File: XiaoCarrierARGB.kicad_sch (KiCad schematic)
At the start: 1 part, among them U1 XIAO-ESP32-C6-DIP

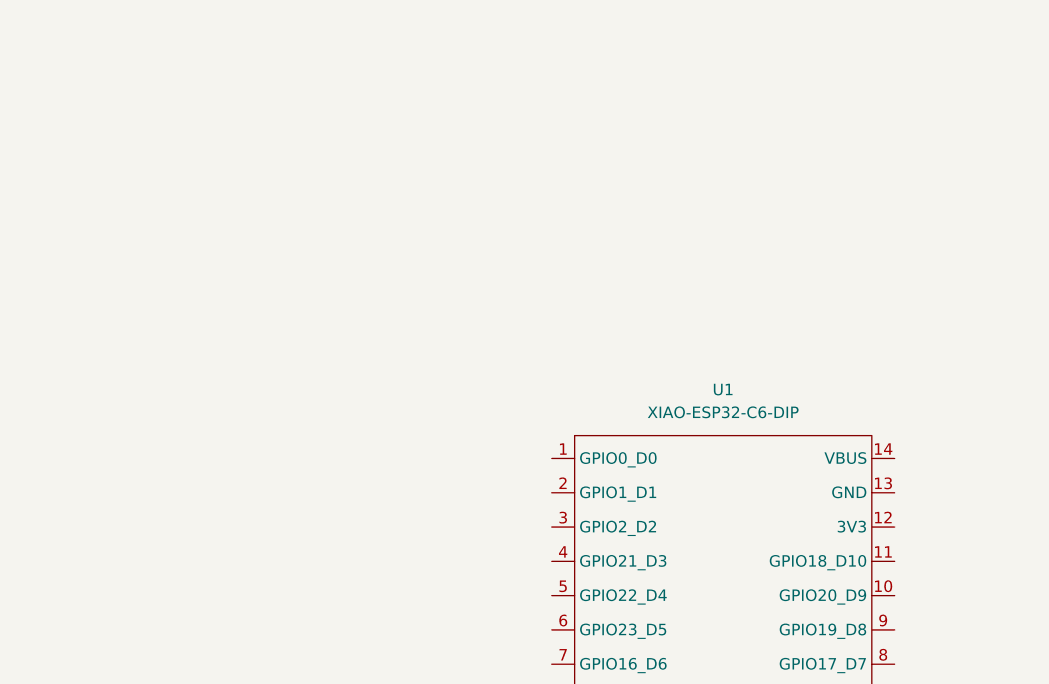
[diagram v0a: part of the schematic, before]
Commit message: Added Buck
TPP362081 added to library and schematic, might switch exact model from TPP362081 to TPP362083
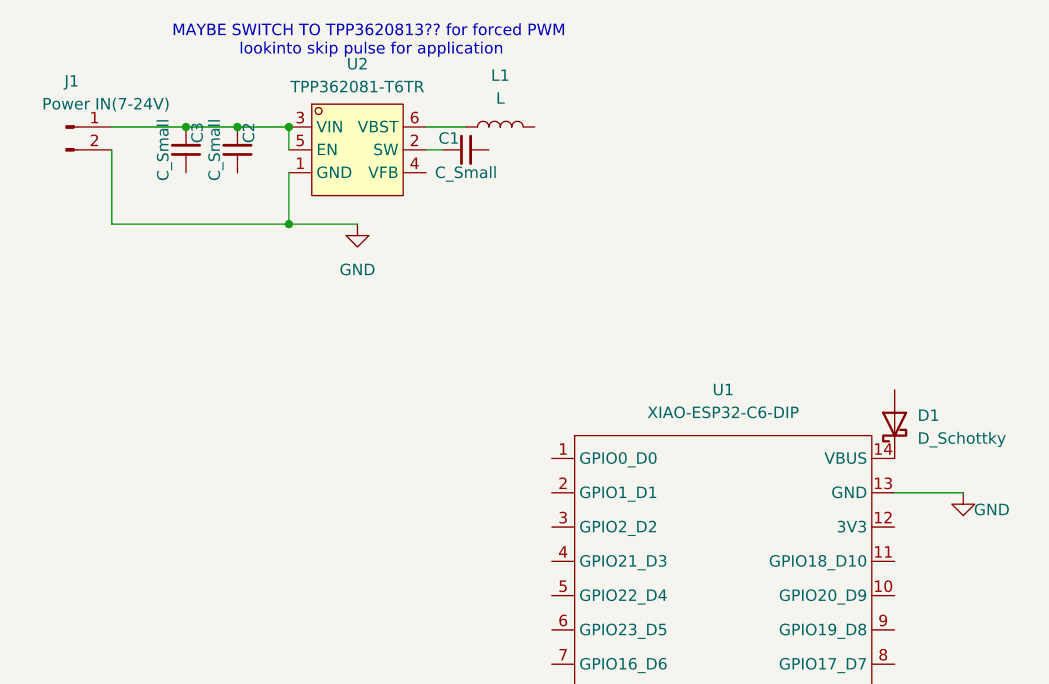
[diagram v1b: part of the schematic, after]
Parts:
- added C1, C2, C3: C_Small, Package_QFP:TQFP-44_10x10mm_P0.8mm, symbol Device:C_Small
- added D1: D_Schottky, Package_SON:WSON-8-1EP_6x5mm_P1.27mm_EP3.4x4mm, symbol Device:D_Schottky
- added J1: Power IN(7-24V), LED_THT:LED_D5.0mm_IRGrey, symbol Connector:Conn_01x02_Pin
- added L1: L, symbol Device:L
- added U2: TPP362081-T6TR, Package_TO_SOT_SMD:TSOT-23-6, symbol EasyEDA:TPP362081-T6TR
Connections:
- net GND: now reaches U1.13 (GND)
- net GND: now also J1.2 (Pin_2), U2.1 (GND)
- net at U1.14 (VBUS): now also D1.1 (K)
- new net: L1.1, U2.6 (VBST)
- new net: C1.1, U2.2 (SW)
- new net: C2.1, C3.1, J1.1 (Pin_1), U2.3 (VIN), U2.5 (EN)
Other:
- note added: "MAYBE SWITCH TO TPP3620813?? for forced PWM lookinto skip pulse for application"

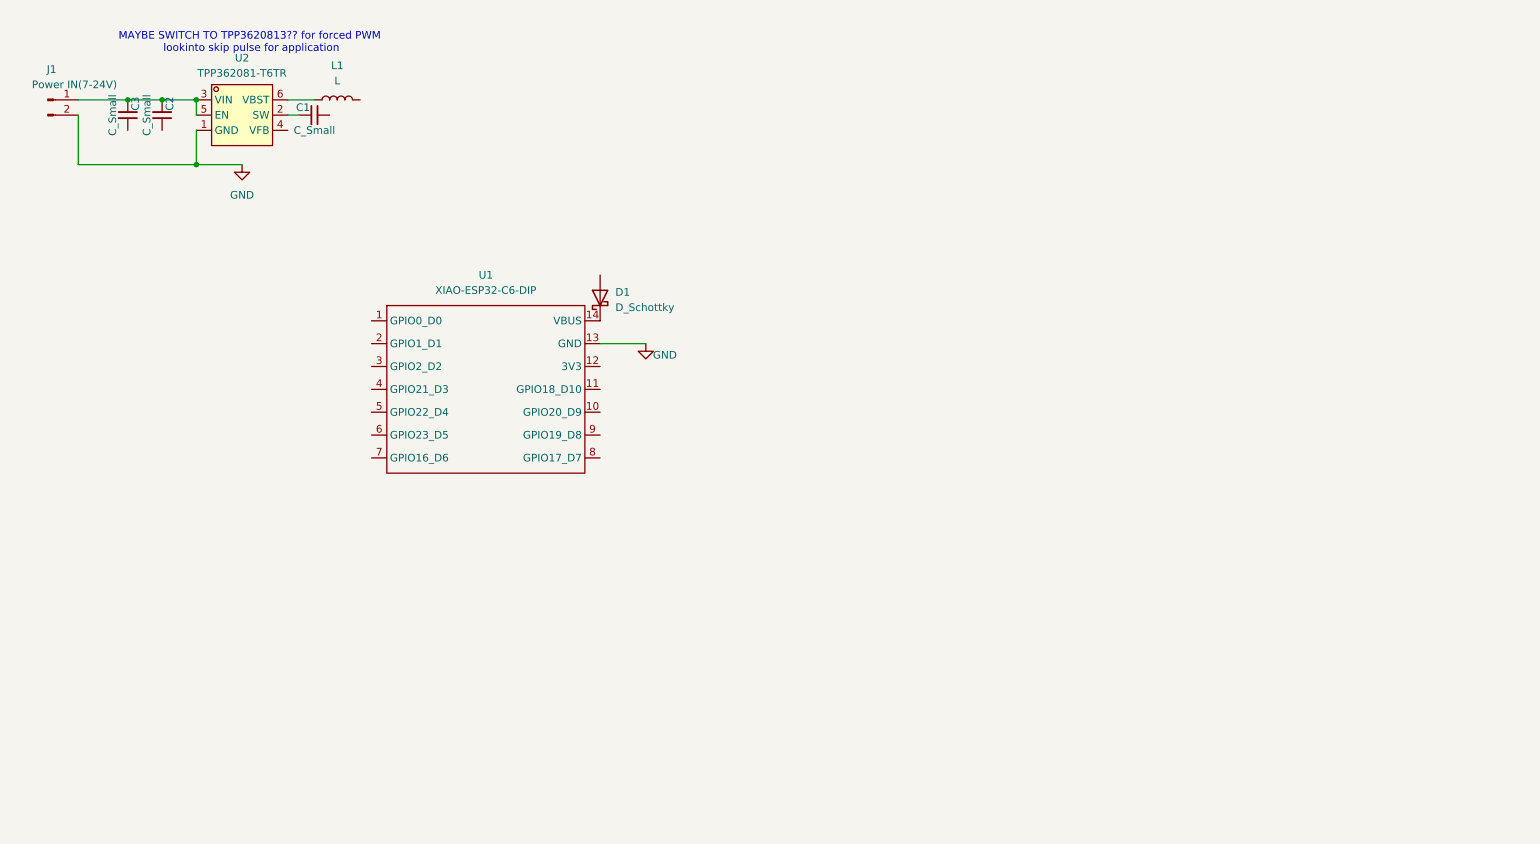
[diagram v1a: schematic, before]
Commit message: added LDO and level shifters.
most footprint assingments done, need to source ptc fuse and decide on if pullups or pulldowns should be placed but not populated for versatility
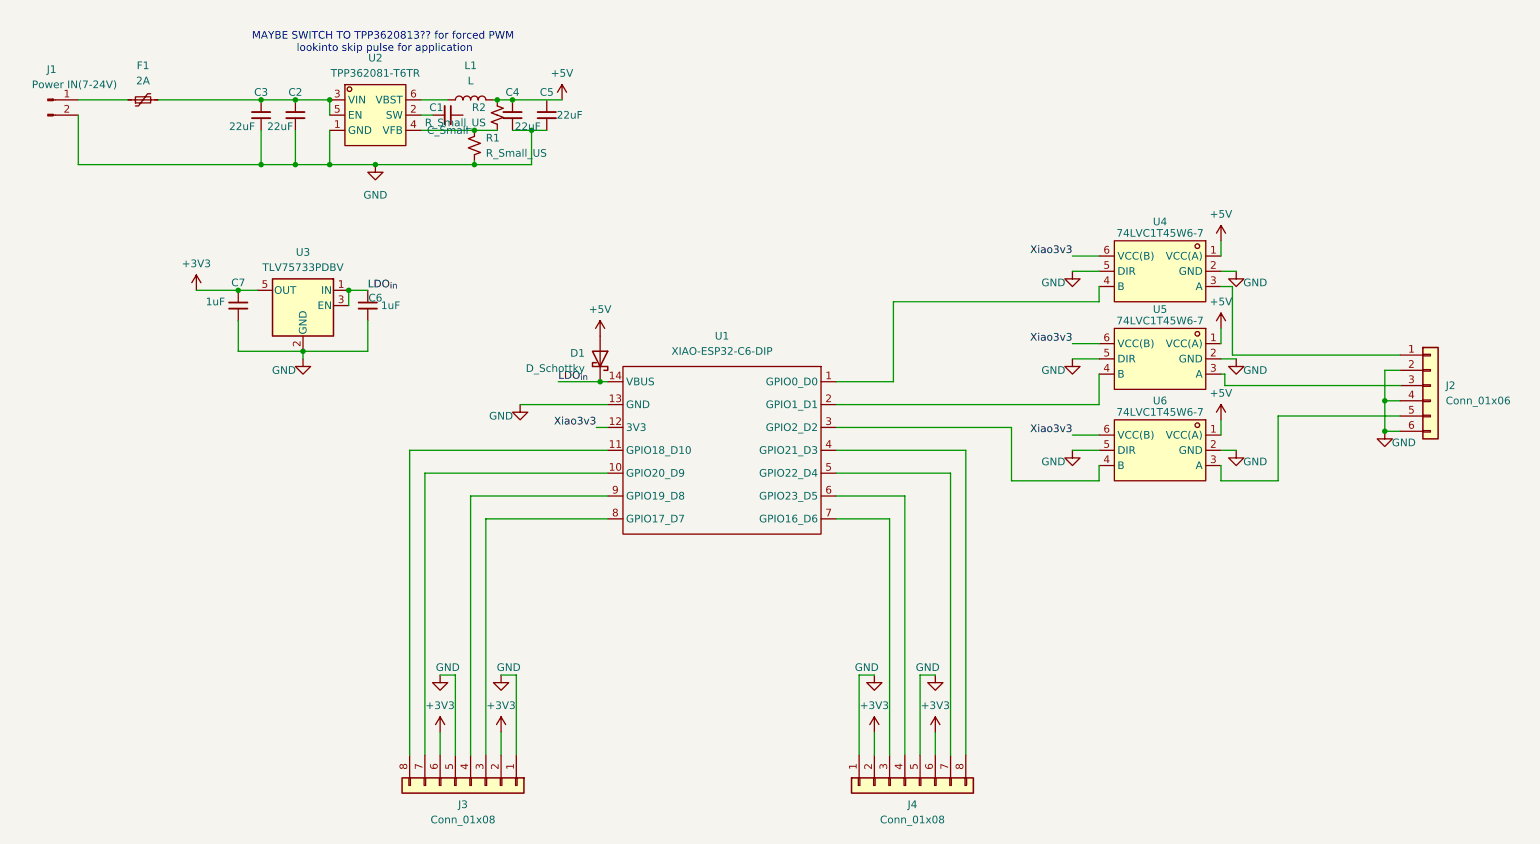
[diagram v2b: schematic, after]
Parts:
- added C4, C5: 22uF, Capacitor_SMD:C_0805_2012Metric_Pad1.18x1.45mm_HandSolder, symbol Device:C_Small
- added C6, C7: 1uF, Capacitor_SMD:C_0805_2012Metric_Pad1.18x1.45mm_HandSolder, symbol Device:C_Small
- added F1: 2A, symbol Device:Polyfuse_Small
- added J2: Conn_01x06, Connector_RJ:RJ45_Abracon_ARJP11A-MA_Horizontal, symbol Connector_Generic:Conn_01x06
- added J3, J4: Conn_01x08, Connector_RJ:RJ45_Abracon_ARJP11A-MA_Horizontal, symbol Connector_Generic:Conn_01x08
- added R1, R2: R_Small_US, Resistor_THT:R_Array_SIP4, symbol Device:R_Small_US
- added U3: TLV75733PDBV, Package_TO_SOT_SMD:SOT-23-5, symbol Regulator_Linear:TLV75733PDBV
- added U4, U5, U6: 74LVC1T45W6-7, Package_TO_SOT_SMD:SOT-23-6, symbol EasyEDA:74LVC1T45W6-7
- C1: footprint Package_QFP:TQFP-44_10x10mm_P0.8mm -> Capacitor_SMD:C_0805_2012Metric_Pad1.18x1.45mm_HandSolder
- C2, C3: value C_Small -> 22uF; footprint Package_QFP:TQFP-44_10x10mm_P0.8mm -> Capacitor_SMD:C_0805_2012Metric_Pad1.18x1.45mm_HandSolder
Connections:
- net GND: now also C2.2, C3.2, C4.2, C5.2, C6.2, C7.2, J2.2 (Pin_2), J2.4 (Pin_4), J2.6 (Pin_6), J3.1 (Pin_1), J3.5 (Pin_5), J4.1 (Pin_1), J4.5 (Pin_5), R1.2, U3.2 (GND), U4.2 (GND), U4.5 (DIR), U5.2 (GND), U5.5 (DIR), U6.2 (GND), U6.5 (DIR)
- net at U1.1 (GPIO0_D0): now also U4.4 (B)
- net at U1.10 (GPIO20_D9): now also J3.7 (Pin_7)
- net at U1.11 (GPIO18_D10): now also J3.8 (Pin_8)
- net Xiao3v3: now reaches U1.12 (3V3)
- net Xiao3v3: now also U4.6 (VCC(B)), U5.6 (VCC(B)), U6.6 (VCC(B))
- net LDO_{in}: now reaches D1.1 (K), U1.14 (VBUS)
- net LDO_{in}: now also C6.1, U3.1 (IN), U3.3 (EN)
- net at U1.2 (GPIO1_D1): now also U5.4 (B)
- net at U1.3 (GPIO2_D2): now also U6.4 (B)
- net at U1.4 (GPIO21_D3): now also J4.8 (Pin_8)
- net at U1.5 (GPIO22_D4): now also J4.7 (Pin_7)
- net at U1.6 (GPIO23_D5): now also J4.4 (Pin_4)
- net at U1.7 (GPIO16_D6): now also J4.3 (Pin_3)
- net at U1.8 (GPIO17_D7): now also J3.3 (Pin_3)
- net at U1.9 (GPIO19_D8): now also J3.4 (Pin_4)
- net +5V: now reaches L1.2
- net +5V: now also D1.2 (A), C4.1, R2.1, U4.1 (VCC(A)), U5.1 (VCC(A)), U6.1 (VCC(A))
- net at C2.1, C3.1, U2.3 (VIN)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: now also F1.2; no longer J1.1 (Pin_1)
- net at U2.4 (VFB): now also R1.1, R2.2
- new net: J2.1 (Pin_1), U4.3 (A)
- new net: J2.3 (Pin_3), U5.3 (A)
- new net: F1.1, J1.1 (Pin_1)
- new net: J2.5 (Pin_5), U6.3 (A)
- new net +3V3: C7.1, J3.2 (Pin_2), J3.6 (Pin_6), J4.2 (Pin_2), J4.6 (Pin_6), U3.5 (OUT)
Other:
- moved on the sheet: C1, C2, C3, D1, L1, U1, U2

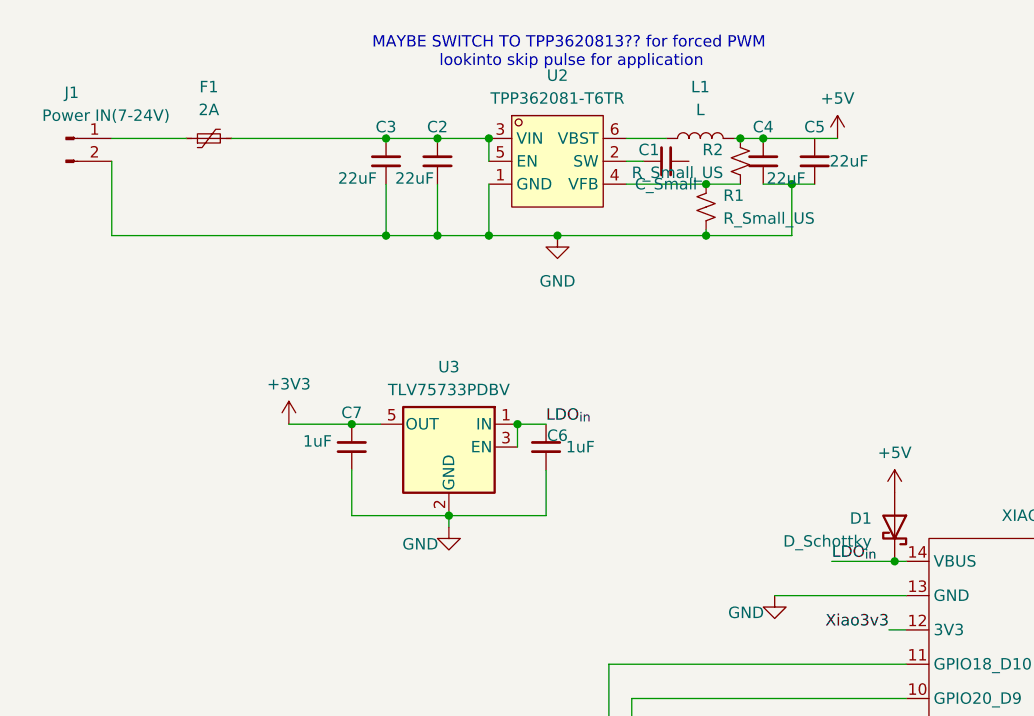
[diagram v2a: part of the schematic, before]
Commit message: Sourced PTC fuse
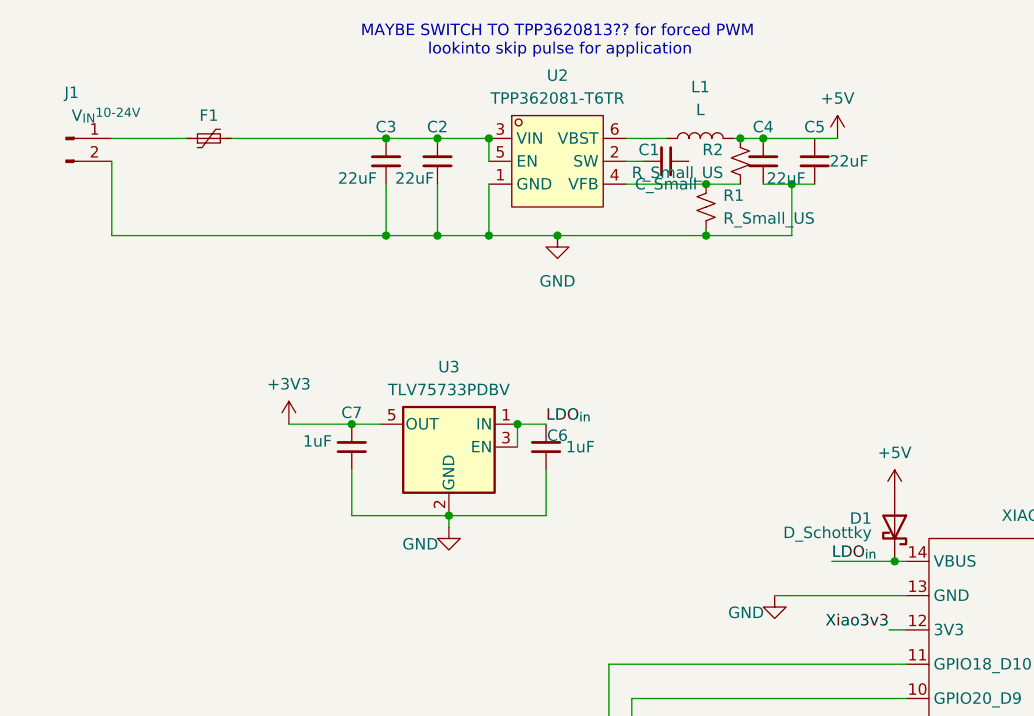
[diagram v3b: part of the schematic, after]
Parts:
- F1: value 2A -> YAGEO SMD1812B110TF/33; footprint (none) -> Fuse:Fuse_1812_4532Metric
- J1: value Power IN(7-24V) -> V_{IN}^{10-24V}
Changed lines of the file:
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@@
 	(text "MAYBE SWITCH TO TPP3620813?? for forced PWM\n lookinto skip pulse for application"
 		(exclude_from_sim no)
-		(at 71.755 30.48 0)
+		(at 70.485 29.21 0)
 		(effects
 			(font
@@
 		(in_pos_files yes)
 		(dnp no)
-		(fields_autoplaced yes)
 		(property "Reference" "F1"
-			(at 31.75 34.29 90)
+			(at 31.75 37.465 90)
 			(show_name no)
 			(do_not_autoplace no)
@@
 			)
 		)
-		(property "Value" "2A"
+		(property "Value" "YAGEO SMD1812B110TF/33"
 			(at 31.75 36.83 90)
+			(hide yes)
 			(show_name no)
 			(do_not_autoplace no)
@@
 			)
 		)
-		(property "Footprint" ""
+		(property "Footprint" "Fuse:Fuse_1812_4532Metric"
 			(at 36.83 38.735 0)
 			(hide yes)
@@
 			)
 		)
-		(property "Datasheet" ""
+		(property "Datasheet" "https://www.mouser.com/datasheet/3/508/1/SMD1812_1.pdf"
 			(at 31.75 40.005 0)
 			(hide yes)
@@
 		(in_pos_files yes)
 		(dnp no)
-		(fields_autoplaced yes)
 		(property "Reference" "D1"
 			(at 105.41 82.2324 90)
@@
 		)
 		(property "Value" "D_Schottky"
-			(at 105.41 84.7724 90)
+			(at 105.41 83.82 90)
 			(show_name no)
 			(do_not_autoplace no)
@@
 			)
 		)
-		(property "Value" "Power IN(7-24V)"
+		(property "Value" "V_{IN}^{10-24V}"
 			(at 20.32 37.465 0)
 			(show_name no)

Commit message: Switched Buck
switched to TPP362083-T6TR to use forced PWM and avoid skip pulse noise
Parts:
- added J5, J6: Conn_01x01, Connector_RJ:RJ45_Abracon_ARJP11A-MA_Horizontal, symbol Connector_Generic:Conn_01x01
- U2: value TPP362081-T6TR -> TPP362083-T6TR; Digikey Part 5503-TPP362081-T6TR -> 5503-TPP362083-T6TR; LCSC Part C29073195 -> C38493766; MPN TPP362081-T6TR -> TPP362083-T6TR
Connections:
- net +5V: now also C5.1, J5.1 (Pin_1), J6.1 (Pin_1)
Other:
- note removed: "MAYBE SWITCH TO TPP3620813?? for forced PWM lookinto skip pulse for application"
- moved on the sheet: C1, C4, C5, L1, R1, R2
